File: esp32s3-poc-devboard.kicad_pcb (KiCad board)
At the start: 4 copper layers, 74 x 66.8 mm, 108 parts, among them J1 24VDC, J2 Conn_01x01_Pin, J3 USB_C_Receptacle_USB2.0_14P, J4 USB_C_Receptacle_USB2.0_14P, J5 Screw_Terminal_01x06, J6 Conn_Coaxial, J7 Conn_01x16_Pin, J8 Screw_Terminal_01x04, Q3 MMDT5551, SW1 SW_Push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

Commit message: xc6206 routing
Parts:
- moved D1 7.05 mm to (186.8, 84.8), turned to 180 degrees
- moved U3 4.82 mm to (183.7, 89.8), turned to 180 degrees
- moved C4 4.81 mm to (186.9, 89.8), turned to -90 degrees
- moved C3 4.51 mm to (183.4, 86.8), turned to 0 degrees
- moved R1 3.81 mm to (186.8, 86.8), turned to 180 degrees
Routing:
- net +5V: track 75.9 -> 89.4 mm
- net Net-(JP2-A): track 0.00 -> 13.2 mm
- net Net-(D1-A): track 0.00 -> 2.07 mm

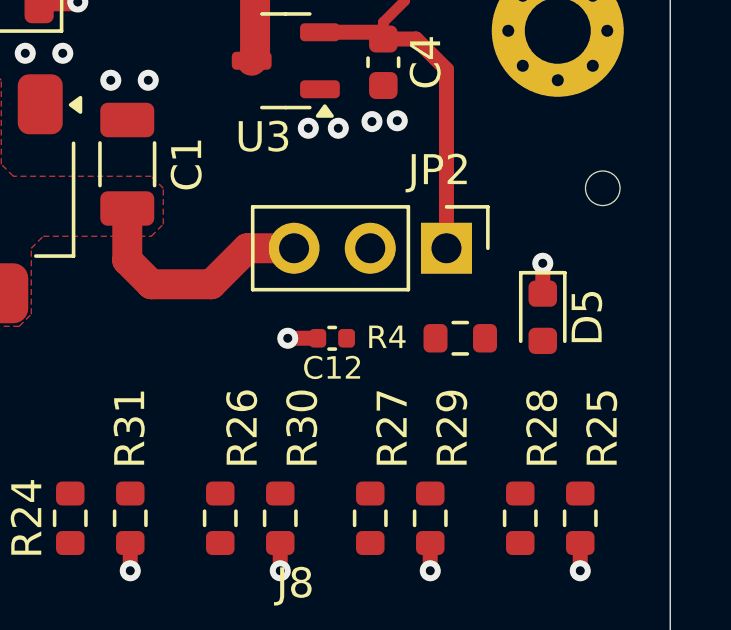
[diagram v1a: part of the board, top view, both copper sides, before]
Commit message: ldo select routing
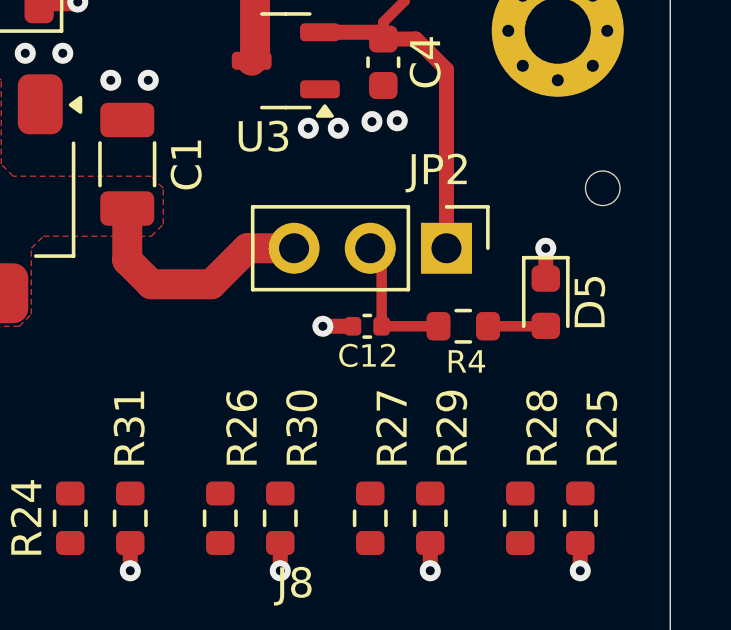
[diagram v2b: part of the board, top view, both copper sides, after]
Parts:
- moved C12 1.24 mm to (186.4, 98.6)
- moved D5 0.51 mm to (192.3, 97.8)
- moved R4 0.41 mm to (189.6, 98.6)
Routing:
- net +3V3: track 0.00 -> 4.65 mm
- net Net-(D5-A): track 0.00 -> 2.05 mm
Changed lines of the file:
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@@
 	(footprint "LED_SMD:LED_0603_1608Metric"
 		(layer "F.Cu")
-		(at 192.25 98.3 -90)
+		(at 192.35 97.8 -90)
 		(descr "LED SMD 0603 (1608 Metric), square (rectangular) end terminal, IPC-7351 nominal, (Body size source: http://www.tortai-tech.com/upload/download/2011102023233369053.pdf), generated with kicad-footprint-generator")
 		(tags "LED")
@@
 	(footprint "Resistor_SMD:R_0603_1608Metric"
 		(layer "F.Cu")
-		(at 189.5 99)
+		(at 189.6 98.6)
 		(descr "Resistor SMD 0603 (1608 Metric), square (rectangular) end terminal, IPC-7351 nominal, (Body size source: IPC-SM-782 page 72, https://www.pcb-3d.com/wordpress/wp-content/uploads/ipc-sm-782a_amendment_1_and_2.pdf), generated with kicad-footprint-generator")
 		(tags "resistor")
 		(property "Reference" "R4"
-			(at -2.451853 -0.02025 0)
+			(at 0.1 1.2 0)
 			(layer "F.SilkS")
 			(effects
@@
 	(footprint "Capacitor_SMD:C_0402_1005Metric"
 		(layer "F.Cu")
-		(at 185.23 99)
+		(at 186.4 98.6)
 		(descr "Capacitor SMD 0402 (1005 Metric), square (rectangular) end terminal, IPC-7351 nominal, (Body size source: IPC-SM-782 page 76, https://www.pcb-3d.com/wordpress/wp-content/uploads/ipc-sm-782a_amendment_1_and_2.pdf), generated with kicad-footprint-generator")
 		(tags "capacitor")
@@
 	)
 	(segment
-		(start 183.75 99)
-		(end 184.57 99)
+		(start 184.92 98.6)
+		(end 185.74 98.6)
 		(width 0.5)
 		(layer "F.Cu")
@@
 	)
 	(segment
-		(start 192.25 96.5)
-		(end 192.25 97.32)
+		(start 192.35 96)
+		(end 192.35 96.82)
 		(width 0.5)
 		(layer "F.Cu")
@@
 	)
 	(via
-		(at 183.75 99)
+		(at 184.92 98.6)
 		(size 0.7)
 		(drill 0.3)
@@
 	)
 	(via
-		(at 192.25 96.5)
+		(at 192.35 96)
 		(size 0.7)
 		(drill 0.3)
@@
 	)
 	(segment
+		(start 186.5 96)
+		(end 186.88 96.38)
+		(width 0.3493)
+		(layer "F.Cu")
+		(net 9)
+	)
+	(segment
+		(start 186.88 96.38)
+		(end 186.88 98.6)
+		(width 0.3493)
+		(layer "F.Cu")
+		(net 9)
+	)
+	(segment
+		(start 186.88 98.6)
+		(end 188.775 98.6)
+		(width 0.3493)
+		(layer "F.Cu")
+		(net 9)
+	)
+	(segment
 		(start 140.8 99.575)
 		(end 142.8 99.575)
@@
 	)
 	(segment
+		(start 190.425 98.6)
+		(end 192.3375 98.6)
+		(width 0.3493)
+		(layer "F.Cu")
+		(net 22)
+	)
+	(segment
+		(start 192.3375 98.6)
+		(end 192.35 98.5875)
+		(width 0.3493)
+		(layer "F.Cu")
+		(net 22)
+	)
+	(segment
+		(start 192.2625 98.5)
+		(end 192.35 98.5875)
+		(width 0.3493)
+		(layer "F.Cu")
+		(net 22)
+	)
+	(segment

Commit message: auto programming routing
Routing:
- net CHIP_PU: track 0.00 -> 91.1 mm
- net BOOT: track 0.00 -> 58.0 mm, vias 0 -> 1
- net Net-(Q3A-B1): track 0.00 -> 3.26 mm
- net Net-(Q3B-B2): track 0.00 -> 3.21 mm
- net Net-(Q3B-C2): track 0.00 -> 1.73 mm
- net Net-(Q3A-C1): track 0.00 -> 1.51 mm

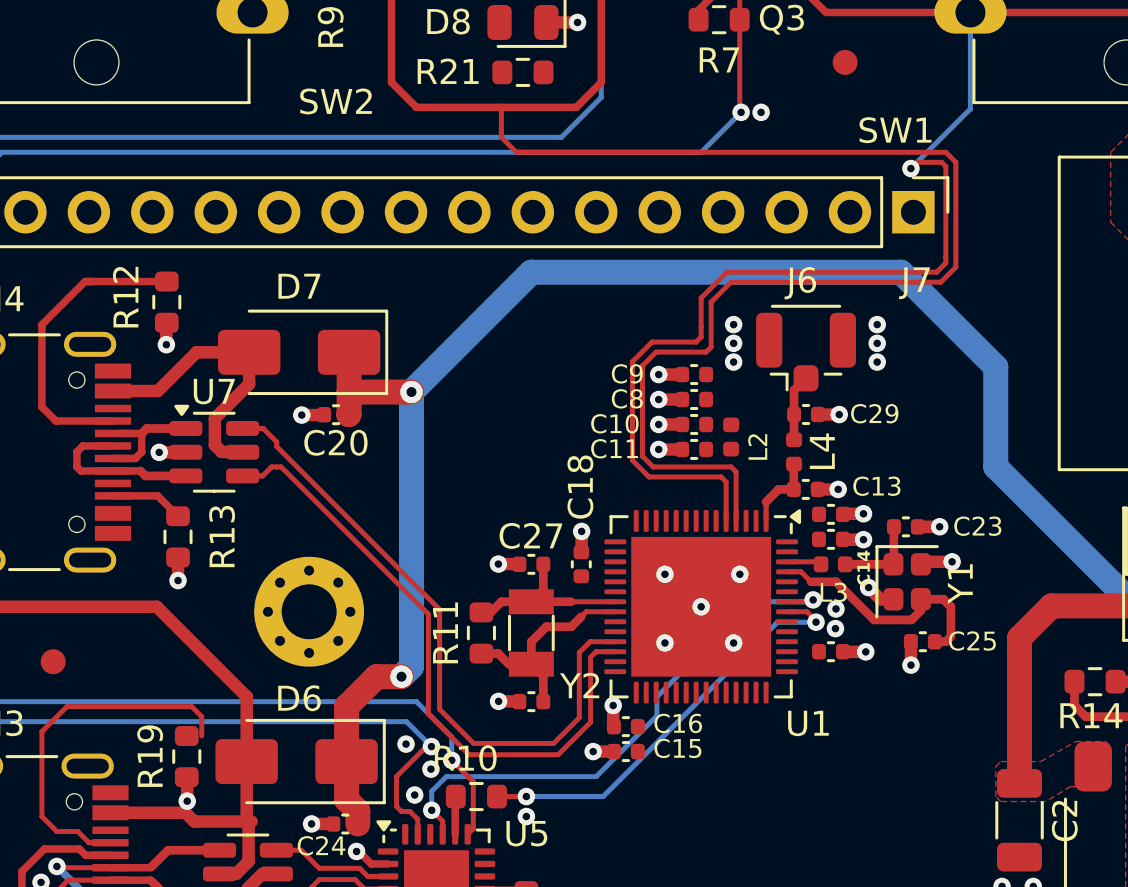
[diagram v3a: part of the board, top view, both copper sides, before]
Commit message: add pin headers routing
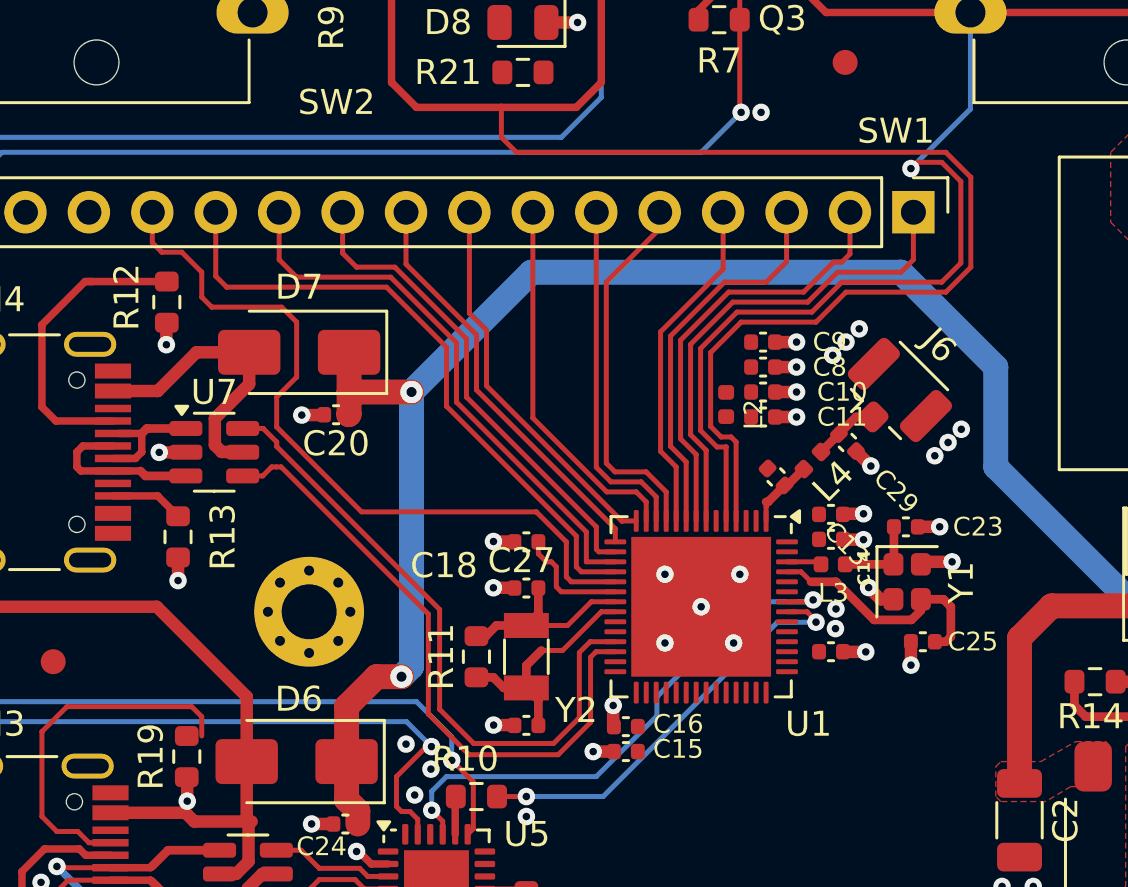
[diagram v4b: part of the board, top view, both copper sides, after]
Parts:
- moved J6 3.89 mm to (162.8, 76.5), turned to 45 degrees
- moved C10 3.05 mm to (157.7, 76.2), turned to 0 degrees
- moved C11 3.05 mm to (157.7, 77.2), turned to 0 degrees
- moved C8 3.05 mm to (157.7, 75.2), turned to 0 degrees
- moved C9 3.05 mm to (157.7, 74.2), turned to 0 degrees
- moved C18 2.38 mm to (148.2, 82.2), turned to 180 degrees
- moved C29 2.00 mm to (161.1, 78.2), turned to -45 degrees
- moved L2 1.32 mm to (156.2, 76.7)
- moved C28 1.29 mm to (158.2, 79.6), turned to 135 degrees
- moved C26 0.97 mm to (148.2, 89.5)
- moved C27 0.97 mm to (148.2, 84.0)
- moved R11 0.97 mm to (146.2, 86.8)
- moved Y2 0.97 mm to (148.2, 86.8)
- moved L4 0.81 mm to (159.7, 78.9), turned to -135 degrees
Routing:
- net Net-(J7-Pin_13): track 0.00 -> 30.4 mm
- net Net-(J7-Pin_12): track 0.00 -> 25.6 mm
- net Net-(J7-Pin_11): track 0.00 -> 22.5 mm
- net Net-(J7-Pin_1): track 0.00 -> 19.6 mm
- net Net-(J7-Pin_10): track 0.00 -> 19.4 mm
- net Net-(J7-Pin_2): track 0.00 -> 17.4 mm
- net Net-(J7-Pin_9): track 0.00 -> 16.7 mm
- net Net-(J7-Pin_3): track 0.00 -> 15.5 mm
- net Net-(J7-Pin_8): track 0.00 -> 15.5 mm
- net Net-(J7-Pin_5): track 0.00 -> 15.0 mm
- net Net-(J7-Pin_7): track 0.00 -> 14.9 mm
- net Net-(J7-Pin_6): track 0.00 -> 14.1 mm
- net Net-(J7-Pin_4): track 0.00 -> 13.7 mm
- net CHIP_PU: track 91.1 -> 85.7 mm
- net BOOT: track 58.0 -> 52.9 mm
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
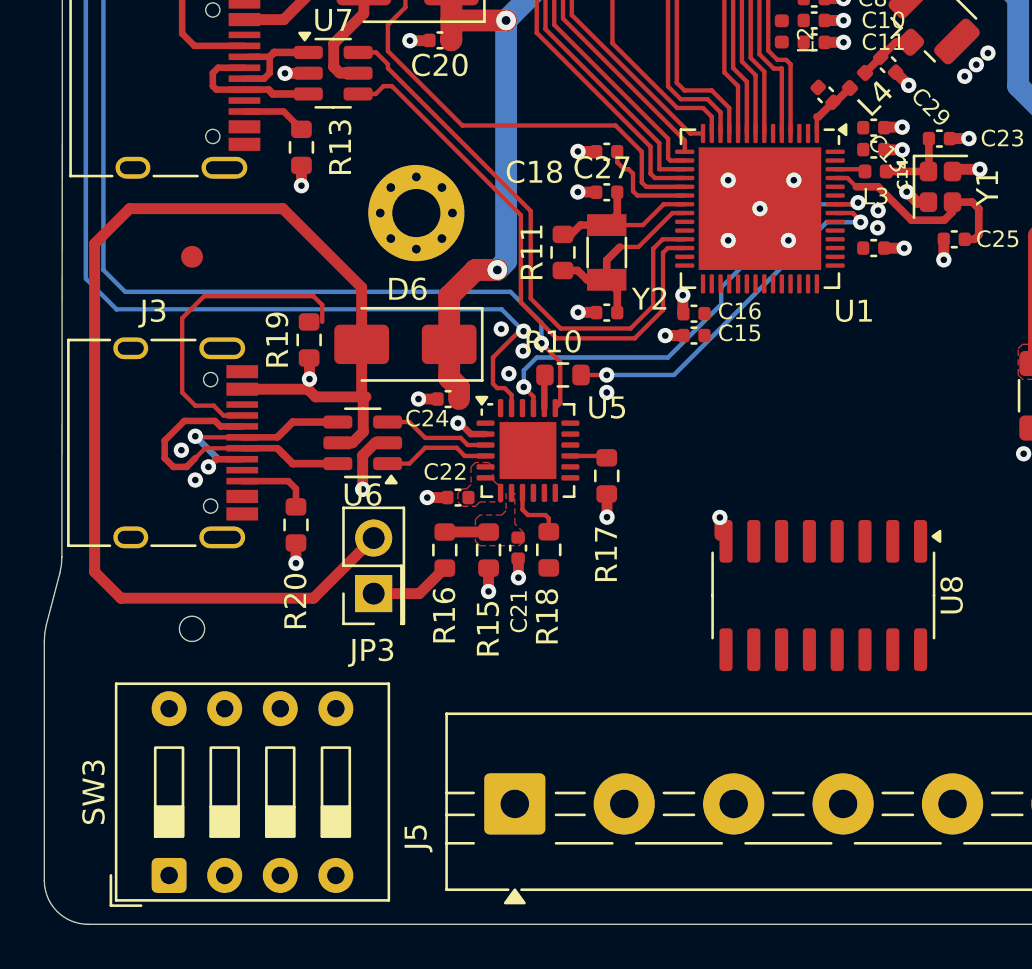
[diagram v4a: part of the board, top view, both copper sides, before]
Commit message: add dip switches routing
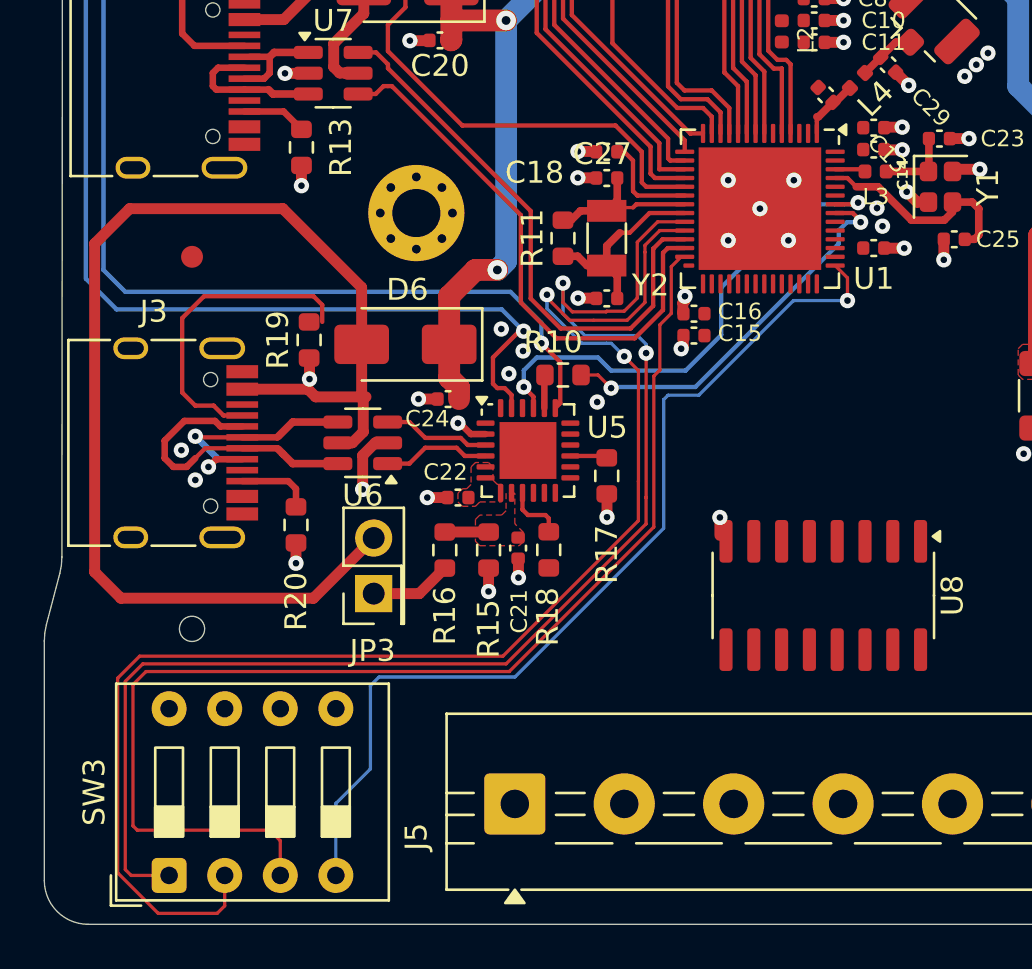
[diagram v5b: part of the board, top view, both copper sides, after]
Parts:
- moved C26 0.65 mm to (148.2, 88.9)
- moved C27 0.65 mm to (148.2, 83.4)
- moved R11 0.65 mm to (146.2, 86.2)
- moved Y2 0.65 mm to (148.2, 86.2)
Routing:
- net GPIO27: track 0.00 -> 65.8 mm, vias 0 -> 2
- net GPIO26: track 0.00 -> 61.3 mm, vias 0 -> 2
- net GPIO28: track 0.00 -> 54.9 mm
- net GPIO29: track 0.00 -> 43.7 mm, vias 0 -> 1
- net U0RXD: track 22.3 -> 23.6 mm
- net Net-(U1-U0TXD/PROG/GPIO43): track 17.4 -> 18.3 mm

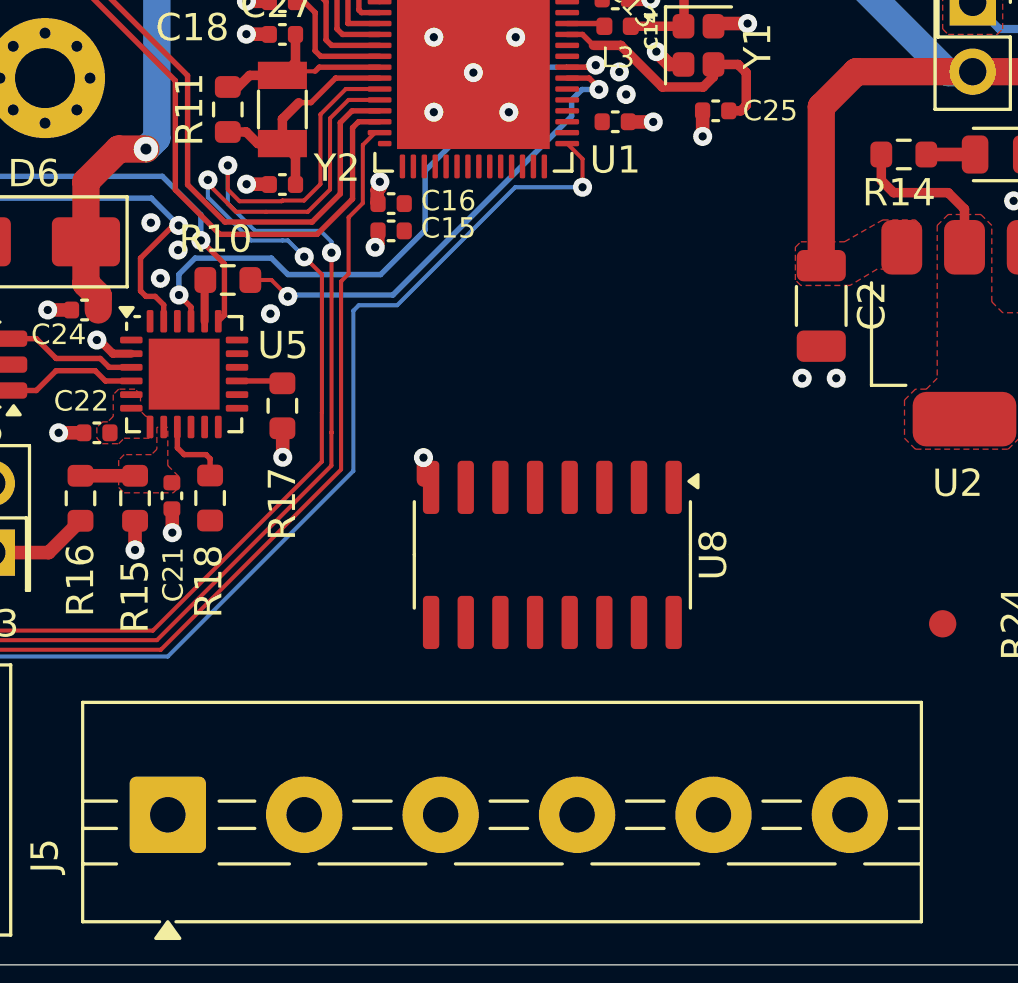
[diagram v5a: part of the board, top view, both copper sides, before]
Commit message: add 24v O routing
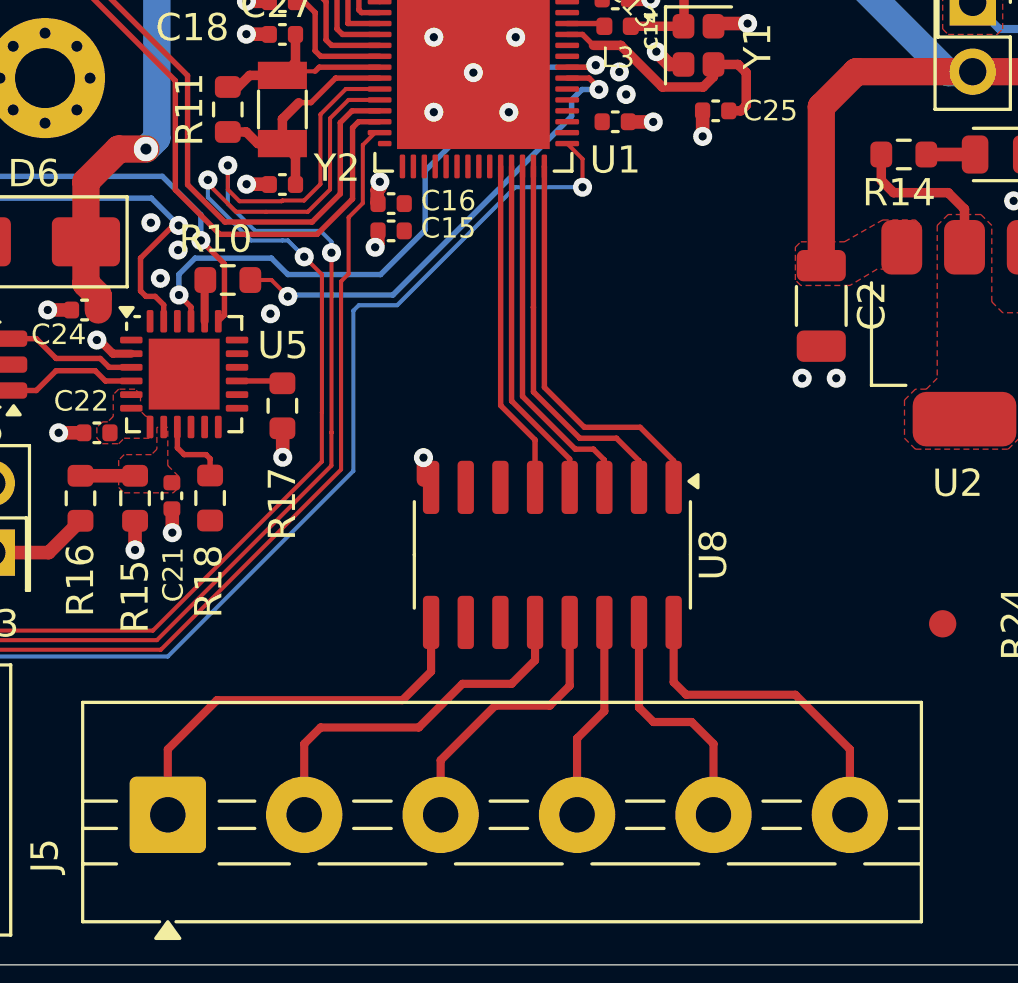
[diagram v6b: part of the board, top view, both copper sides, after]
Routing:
- net Net-(J5-Pin_1): track 0.00 -> 15.0 mm
- net Net-(U1-GPIO37): track 0.00 -> 14.9 mm
- net Net-(U1-GPIO36): track 0.00 -> 14.2 mm
- net Net-(J5-Pin_2): track 0.00 -> 13.7 mm
- net Net-(U1-GPIO35): track 0.00 -> 13.4 mm
- net Net-(U1-GPIO34): track 0.00 -> 12.6 mm
- net Net-(U1-GPIO33): track 0.00 -> 12.3 mm
- net Net-(J5-Pin_6): track 0.00 -> 12.1 mm
- net Net-(J5-Pin_3): track 0.00 -> 10.2 mm
- net Net-(J5-Pin_5): track 0.00 -> 9.00 mm
- net Net-(J5-Pin_4): track 0.00 -> 7.46 mm
